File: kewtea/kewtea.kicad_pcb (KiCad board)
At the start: 2 copper layers, 192 x 85 mm, 62 parts, among them J1 OLED_128x32, U1 Nice_Nano_V2

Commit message: add generated drill files for pcb
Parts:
- moved D13 0.05 mm to (93.8, 73.0)
- moved D16 0.05 mm to (148.1, 73.2)
- moved D28 0.05 mm to (201.6, 90.4)
- moved D29 0.05 mm to (219.6, 90.4)
- moved D1 0.05 mm to (75.5, 55.8)
- moved D10 0.05 mm to (237.7, 55.6)
- moved D2 0.05 mm to (93.5, 56.1)
- moved D3 0.05 mm to (111.6, 56.1)
- moved D9 0.05 mm to (219.6, 55.7)

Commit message: fix pcb zone fill issues
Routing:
- net SDA: track 133.1 -> 132.6 mm
- net ROW1: track 387.4 -> 387.9 mm

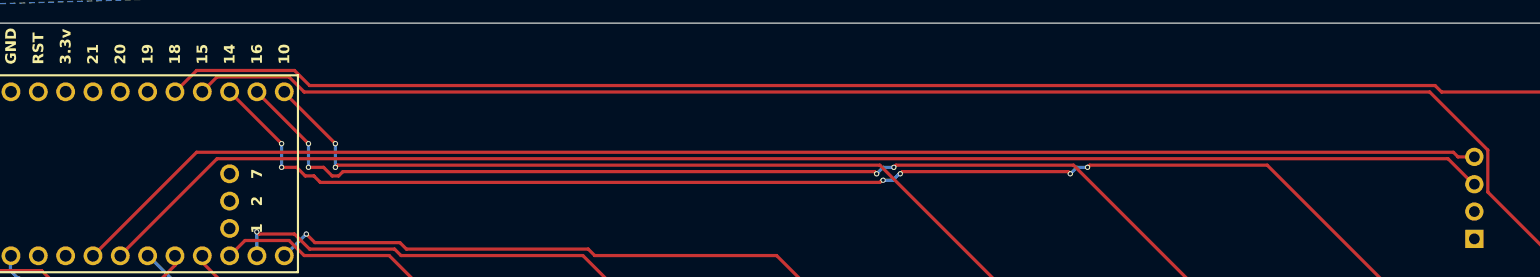
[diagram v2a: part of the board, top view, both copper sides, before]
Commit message: fix unrouted vcc from nice!nano to 128x32 oled
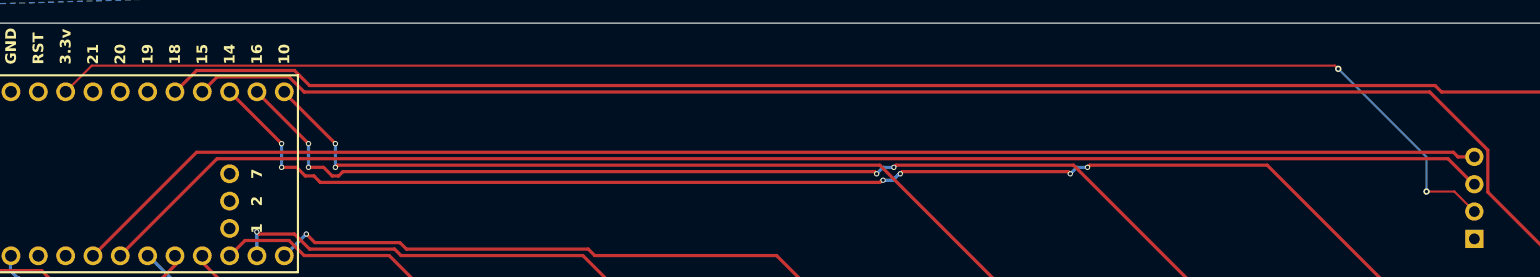
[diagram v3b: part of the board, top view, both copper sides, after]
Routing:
- net VCC: track 0.00 -> 139.4 mm, vias 0 -> 2
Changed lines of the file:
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@@
+	)
+	(segment
+		(start 66.36 18.95)
+		(end 181.9 18.95)
+		(width 0.2)
+		(layer "F.Cu")
+		(net "VCC")
+	)
+	(segment
+		(start 63.93 21.38)
+		(end 66.36 18.95)
+		(width 0.2)
+		(layer "F.Cu")
+		(net "VCC")
+	)
+	(segment
+		(start 192.99 30.65)
+		(end 194.85 32.51)
+		(width 0.2)
+		(layer "F.Cu")
+		(net "VCC")
+	)
+	(segment
+		(start 181.9 18.95)
+		(end 182.2 19.25)
+		(width 0.2)
+		(layer "F.Cu")
+		(net "VCC")
+	)
+	(segment
+		(start 190.4 30.65)
+		(end 192.99 30.65)
+		(width 0.2)
+		(layer "F.Cu")
+		(net "VCC")
+	)
+	(via
+		(at 182.2 19.25)
+		(size 0.6)
+		(drill 0.3)
+		(layers "F.Cu" "B.Cu")
+		(net "VCC")
+	)
+	(via
+		(at 190.4 30.65)
+		(size 0.6)
+		(drill 0.3)
+		(layers "F.Cu" "B.Cu")
+		(net "VCC")
+	)
+	(segment
+		(start 182.2 19.25)
+		(end 190.4 27.45)
+		(width 0.2)
+		(layer "B.Cu")
+		(net "VCC")
+	)
+	(segment
+		(start 190.4 27.45)
+		(end 190.4 30.65)
+		(width 0.2)
+		(layer "B.Cu")
+		(net "VCC")
 	)
 	(segment
@@
 		(hatch edge 0.5)
 		(connect_pads
-			(clearance 0.5)
+			(clearance 0.3)
 		)
 		(min_thickness 0.25)
 		(fill yes
-			(thermal_gap 0.5)
-			(thermal_bridge_width 0.5)
+			(thermal_gap 0.25)
+			(thermal_bridge_width 0.3)
 			(island_removal_mode 0)
 		)
@@
 		(hatch edge 0.5)
 		(priority 1)
-		(connect_pads
-			(clearance 0.5)
-		)
-		(min_thickness 0.25)
+		(connect_pads yes
+			(clearance 0.2)
+		)
+		(min_thickness 0.1)
 		(fill yes
 			(thermal_gap 0.5)
 			(thermal_bridge_width 0.5)
-			(island_removal_mode 0)
+			(island_removal_mode 1)
 		)
 		(polygon

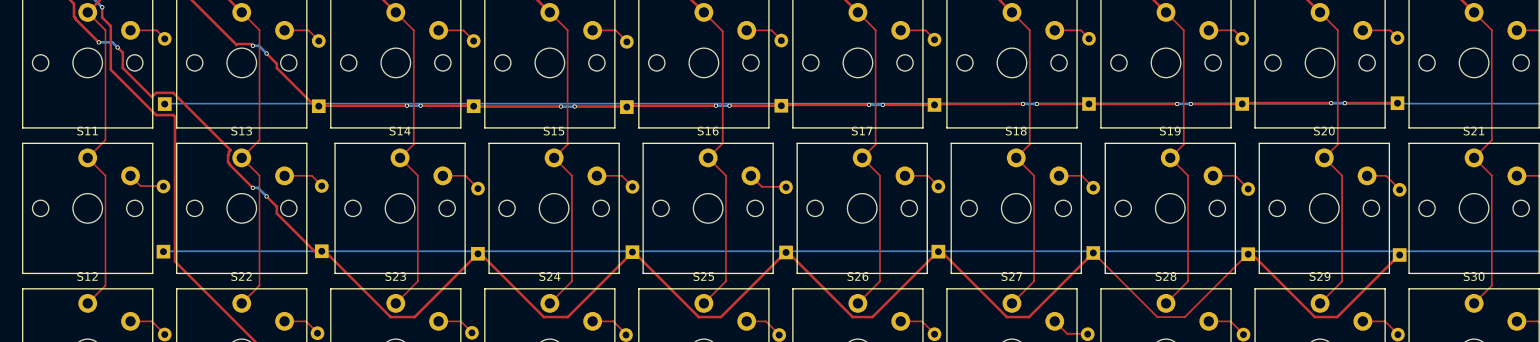
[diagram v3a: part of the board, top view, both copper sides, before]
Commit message: fix silkscreen and bad routing
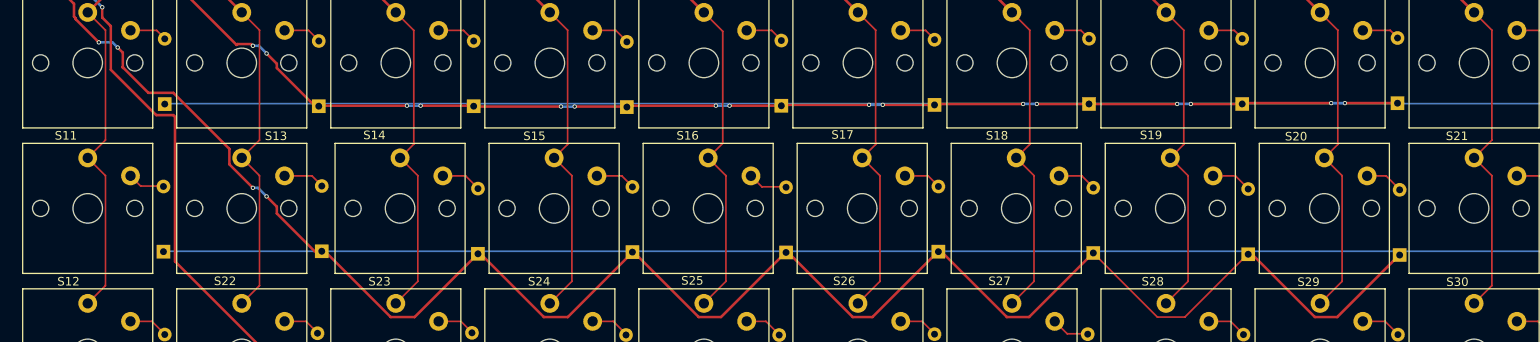
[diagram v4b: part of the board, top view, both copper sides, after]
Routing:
- net ROW1: track 387.9 -> 387.4 mm
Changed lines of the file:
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@@
 		(tags "Choc Keyswitch Switch CPG1350 V1 Cutout")
 		(property "Reference" "S19"
-			(at 0 -9 0)
+			(at -2.25 -8.55 0)
 			(layer "F.SilkS")
 			(effects
@@
 		(tags "Choc Keyswitch Switch CPG1350 V1 Cutout")
 		(property "Reference" "S16"
-			(at 0 -9 0)
+			(at -2.4 -8.5 0)
 			(layer "F.SilkS")
 			(effects
@@
 		(tags "Choc Keyswitch Switch CPG1350 V1 Cutout")
 		(property "Reference" "S22"
-			(at 0 -9 0)
+			(at -1.95 -8.5 0)
 			(layer "F.SilkS")
 			(effects
@@
 		(tags "Choc Keyswitch Switch CPG1350 V1 Cutout")
 		(property "Reference" "S30"
-			(at 0 -9 0)
+			(at -1.95 -8.4 0)
 			(layer "F.SilkS")
 			(effects
@@
 		(tags "Choc Keyswitch Switch CPG1350 V1 Cutout")
 		(property "Reference" "S14"
-			(at 0 -9 0)
+			(at -3 -8.55 0)
 			(layer "F.SilkS")
 			(effects
@@
 		(tags "Choc Keyswitch Switch CPG1350 V1 Cutout")
 		(property "Reference" "S23"
-			(at 0 -9 0)
+			(at -1.9 -8.45 0)
 			(layer "F.SilkS")
 			(effects
@@
 		(tags "Choc Keyswitch Switch CPG1350 V1 Cutout")
 		(property "Reference" "S15"
-			(at 0 -9 0)
+			(at -2.3 -8.45 0)
 			(layer "F.SilkS")
 			(effects
@@
 		(tags "Choc Keyswitch Switch CPG1350 V1 Cutout")
 		(property "Reference" "S26"
-			(at 0 -9 0)
+			(at -1.6 -8.5 0)
 			(layer "F.SilkS")
 			(effects
@@
 		(tags "Choc Keyswitch Switch CPG1350 V1 Cutout")
 		(property "Reference" "S20"
-			(at 0 -9 0)
+			(at -3.3 -8.4 0)
 			(layer "F.SilkS")
 			(effects
@@
 		(tags "Choc Keyswitch Switch CPG1350 V1 Cutout")
 		(property "Reference" "S12"
-			(at 0 -9 0)
+			(at -2.25 -8.45 0)
 			(layer "F.SilkS")
 			(effects
@@
 		(tags "Choc Keyswitch Switch CPG1350 V1 Cutout")
 		(property "Reference" "S25"
-			(at 0 -9 0)
+			(at -1.35 -8.55 0)
 			(layer "F.SilkS")
 			(effects
@@
 		(tags "Choc Keyswitch Switch CPG1350 V1 Cutout")
 		(property "Reference" "S17"
-			(at 0 -9 0)
+			(at -2.3 -8.6 0)
 			(layer "F.SilkS")
 			(effects
@@
 		(tags "Choc Keyswitch Switch CPG1350 V1 Cutout")
 		(property "Reference" "S13"
-			(at 0 -9 0)
+			(at 4 -8.45 0)
 			(layer "F.SilkS")
 			(effects
@@
 		(tags "Choc Keyswitch Switch CPG1350 V1 Cutout")
 		(property "Reference" "S28"
-			(at 0 -9 0)
+			(at -1.55 -8.45 0)
 			(layer "F.SilkS")
 			(effects
@@
 		(tags "Choc Keyswitch Switch CPG1350 V1 Cutout")
 		(property "Reference" "S27"
-			(at 0 -9 0)
+			(at -1.45 -8.5 0)
 			(layer "F.SilkS")
 			(effects
@@
 		(tags "Choc Keyswitch Switch CPG1350 V1 Cutout")
 		(property "Reference" "S24"
-			(at 0 -9 0)
+			(at -1.25 -8.45 0)
 			(layer "F.SilkS")
 			(effects
@@
 		(tags "Choc Keyswitch Switch CPG1350 V1 Cutout")
 		(property "Reference" "S18"
-			(at 0 -9 0)
+			(at -2.25 -8.5 0)
 			(layer "F.SilkS")
 			(effects
@@
 		(tags "Choc Keyswitch Switch CPG1350 V1 Cutout")
 		(property "Reference" "S11"
-			(at 0 -9 0)
+			(at -2.55 -8.5 0)
 			(layer "F.SilkS")
 			(effects
@@
 		(tags "Choc Keyswitch Switch CPG1350 V1 Cutout")
 		(property "Reference" "S21"
-			(at 0 -9 0)
+			(at -2 -8.45 0)
 			(layer "F.SilkS")
 			(effects
@@
 		(tags "Choc Keyswitch Switch CPG1350 V1 Cutout")
 		(property "Reference" "S29"
-			(at 0 -9 0)
+			(at -1.35 -8.4 0)
 			(layer "F.SilkS")
 			(effects
@@
 	)
 	(segment
-		(start 82.9 62.6)
-		(end 83.1 62.8)
-		(width 0.3)
-		(layer "F.Cu")
-		(net "ROW1")
-	)
-	(segment
-		(start 74.5 54.5)
-		(end 76.5 54.5)
+		(start 76.5 54.5)
+		(end 83.05 61.05)
 		(width 0.3)
 		(layer "F.Cu")
@@
 	)
 	(segment
-		(start 83.1 62.9)
-		(end 85.8 65.599999)
+		(start 70.6 51.45)
+		(end 70.6 51.6)
 		(width 0.3)
 		(layer "F.Cu")
@@
 	)
 	(segment
+		(start 70.6 51.509188)
+		(end 73.590812 54.5)
+		(width 0.3)
+		(layer "F.Cu")
+		(net "ROW1")
+	)
+	(segment
 		(start 148.1 73.1)
 		(end 148.3 73.1)
@@
 	)
 	(segment
-		(start 82.9 61.8)
-		(end 82.9 62.6)
-		(width 0.3)
-		(layer "F.Cu")
-		(net "ROW1")
-	)
-	(segment
-		(start 184 73.2)
-		(end 184.1 73.3)
+		(start 83.05 62.85)
+		(end 85.8 65.599999)
 		(width 0.3)
 		(layer "F.Cu")
@@
 	)
 	(segment
-		(start 76.5 54.5)
-		(end 83.2 61.2)
+		(start 73.590812 54.5)
+		(end 76.5 54.5)
 		(width 0.3)
 		(layer "F.Cu")
@@
 	)
 	(segment
-		(start 70.6 49.8)
-		(end 70.6 51.6)
+		(start 184 73.2)
+		(end 184.1 73.3)
 		(width 0.3)
 		(layer "F.Cu")
@@
 	)
 	(segment
+		(start 70.6 49.8)
+		(end 70.6 51.45)
+		(width 0.3)
+		(layer "F.Cu")
+		(net "ROW1")
+	)
+	(segment
 		(start 184.1 73.3)
 		(end 184.5 73.3)
@@
 	)
 	(segment
-		(start 83 61.4)
-		(end 83 61.7)
-		(width 0.3)
-		(layer "F.Cu")
-		(net "ROW1")
-	)
-	(segment
 		(start 88.6 68.6)
 		(end 93 73)
@@
 	)
 	(segment
-		(start 74 55)
-		(end 74.5 54.5)
-		(width 0.3)
-		(layer "F.Cu")
-		(net "ROW1")
-	)
-	(segment
 		(start 101.9 80.7)
 		(end 104.7 80.7)
@@
 	)
 	(segment
-		(start 83.2 61.2)
-		(end 83 61.4)
-		(width 0.3)
-		(layer "F.Cu")
-		(net "ROW1")
-	)
-	(segment
 		(start 130.199999 73.1)
 		(end 130.3 73.1)
@@
 	)
 	(segment
-		(start 70 49.2)
-		(end 70.6 49.8)
+		(start 88.6 67.8)
+		(end 88.6 68.6)
 		(width 0.3)
 		(layer "F.Cu")
@@
 	)
 	(segment
-		(start 88.6 67.8)
-		(end 88.6 68.6)
-		(width 0.3)
+		(start 191.49 80.7)
+		(end 194.7 80.7)
+		(width 0.2)
 		(layer "F.Cu")
 		(net "ROW1")
 	)
 	(segment
-		(start 83 61.7)
-		(end 82.9 61.8)
+		(start 94.1 73.3)
+		(end 94.5 73.3)
 		(width 0.3)
 		(layer "F.Cu")
@@
 	)
 	(segment
-		(start 191.49 80.7)
-		(end 194.7 80.7)
-		(width 0.2)
+		(start 140.5 80.7)
+		(end 148.1 73.1)
+		(width 0.3)
 		(layer "F.Cu")
 		(net "ROW1")
 	)
 	(segment
-		(start 70.6 51.6)
-		(end 74 55)
+		(start 202.2 73.4)
+		(end 202.6 73.4)
 		(width 0.3)
 		(layer "F.Cu")
@@
 	)
 	(segment
-		(start 94.1 73.3)
-		(end 94.5 73.3)
+		(start 83.05 61.05)
+		(end 83.05 62.85)
 		(width 0.3)
 		(layer "F.Cu")
@@
 	)
 	(segment
-		(start 140.5 80.7)
-		(end 148.1 73.1)
+		(start 212.5 80.7)
+		(end 219.8 73.4)
 		(width 0.3)
 		(layer "F.Cu")
@@
 	)
 	(segment
-		(start 202.2 73.4)
-		(end 202.6 73.4)
+		(start 70 49.2)
+		(end 70.6 49.8)
 		(width 0.3)
 		(layer "F.Cu")
@@
 	)
 	(segment
-		(start 212.5 80.7)
-		(end 219.8 73.4)
+		(start 70.6 51.45)
+		(end 70.6 51.509188)
 		(width 0.3)
 		(layer "F.Cu")
@@
 		(width 0.3)
 		(layer "F.Cu")
-		(net "ROW1")
-	)
-	(segment
-		(start 83.1 62.8)
-		(end 83.1 62.9)
-		(width 0.3)
-		(layer "F.Cu")

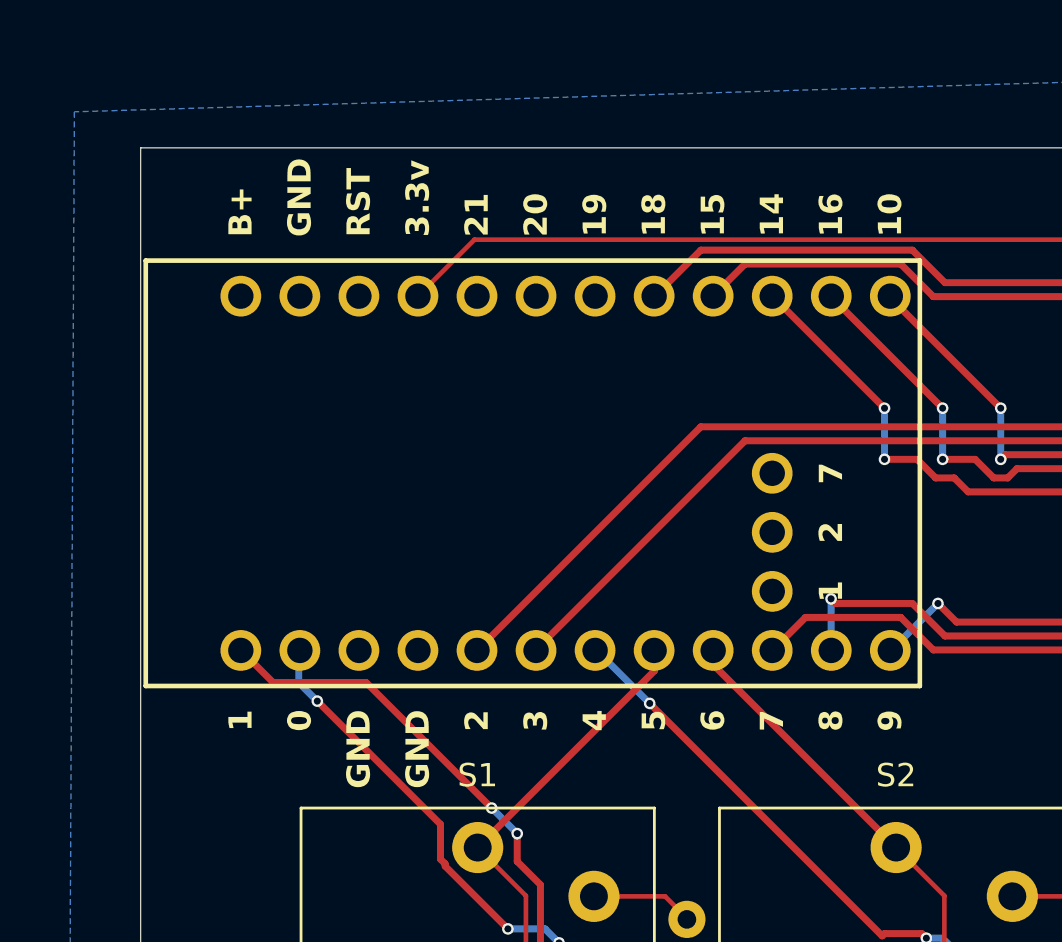
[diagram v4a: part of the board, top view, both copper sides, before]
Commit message: update dimensions for pcb
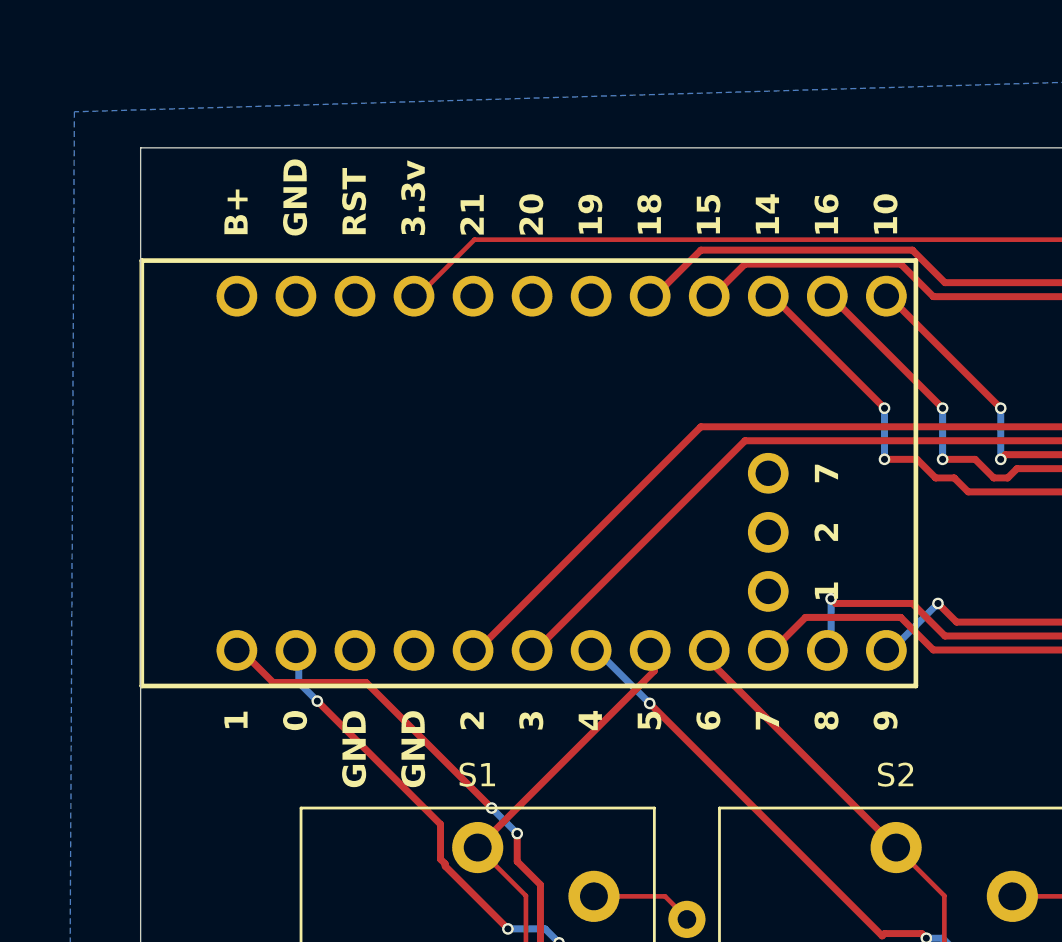
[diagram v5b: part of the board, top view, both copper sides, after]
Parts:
- moved U1 0.17 mm to (69.8, 29.0)
